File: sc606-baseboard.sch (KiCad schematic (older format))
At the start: 0 parts

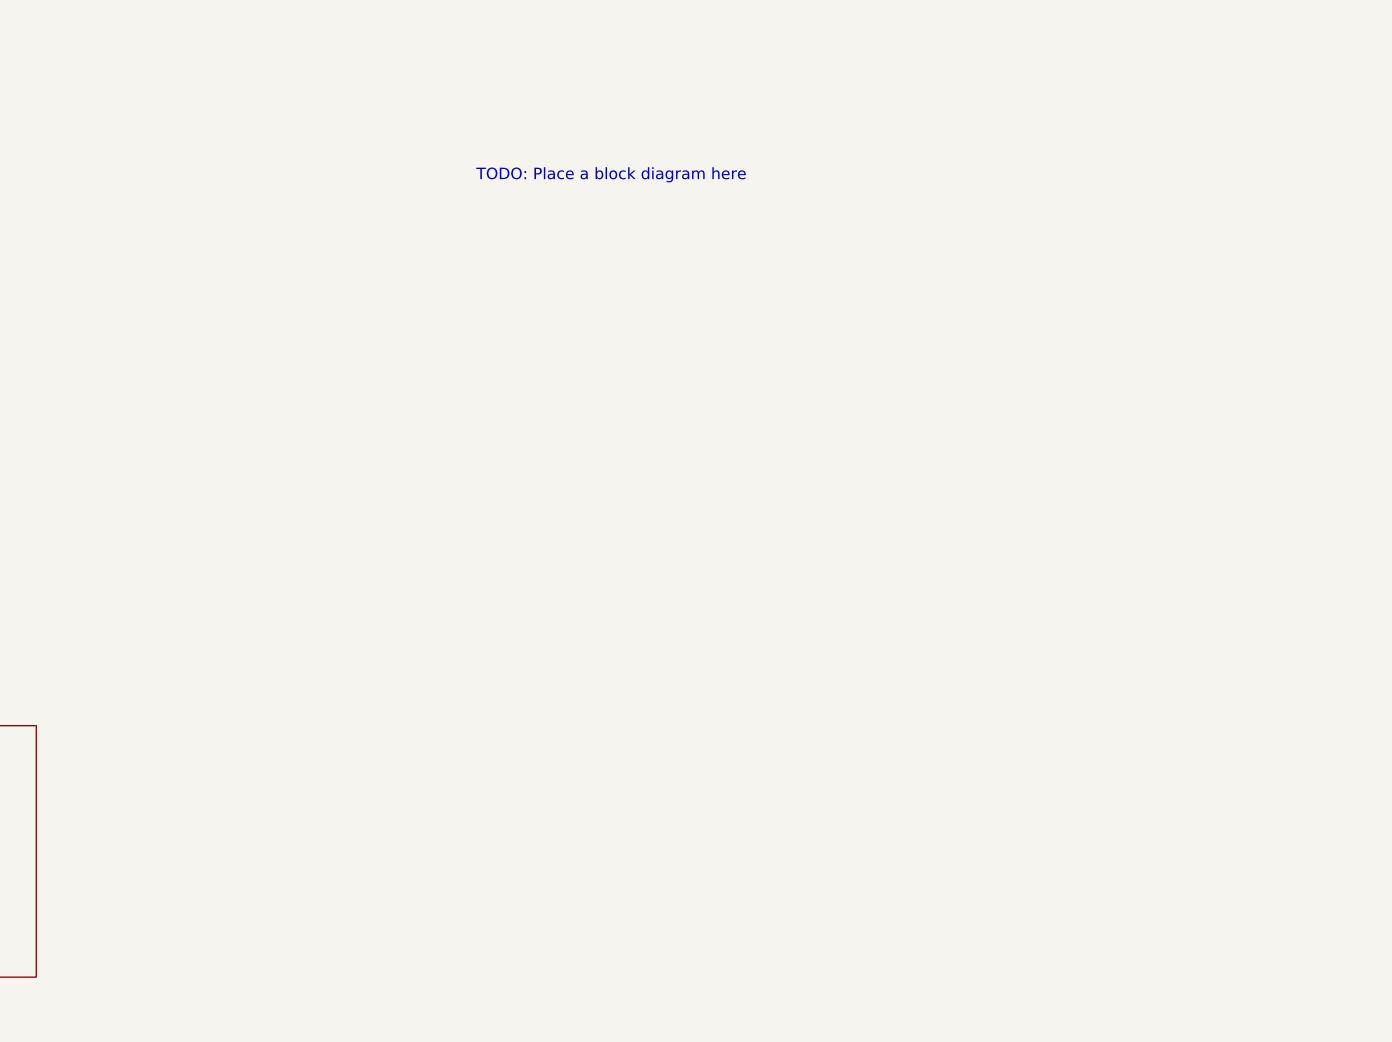
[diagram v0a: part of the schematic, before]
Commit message: update of block diagram, creation of sub-sheets
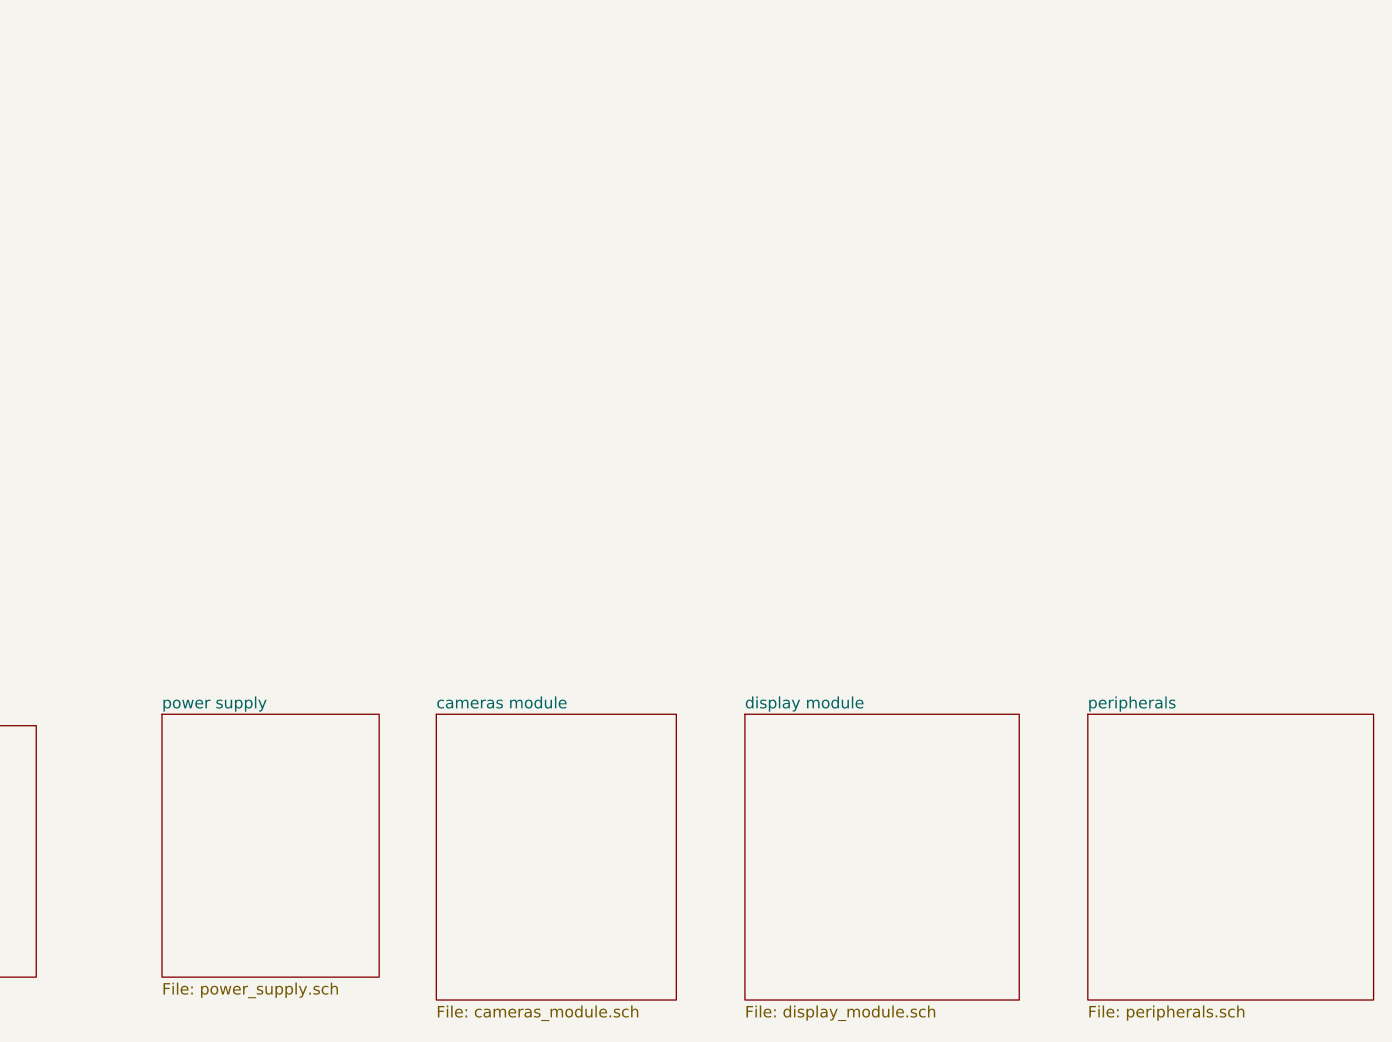
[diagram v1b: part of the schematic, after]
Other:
- note removed: "TODO: Place a block diagram here"

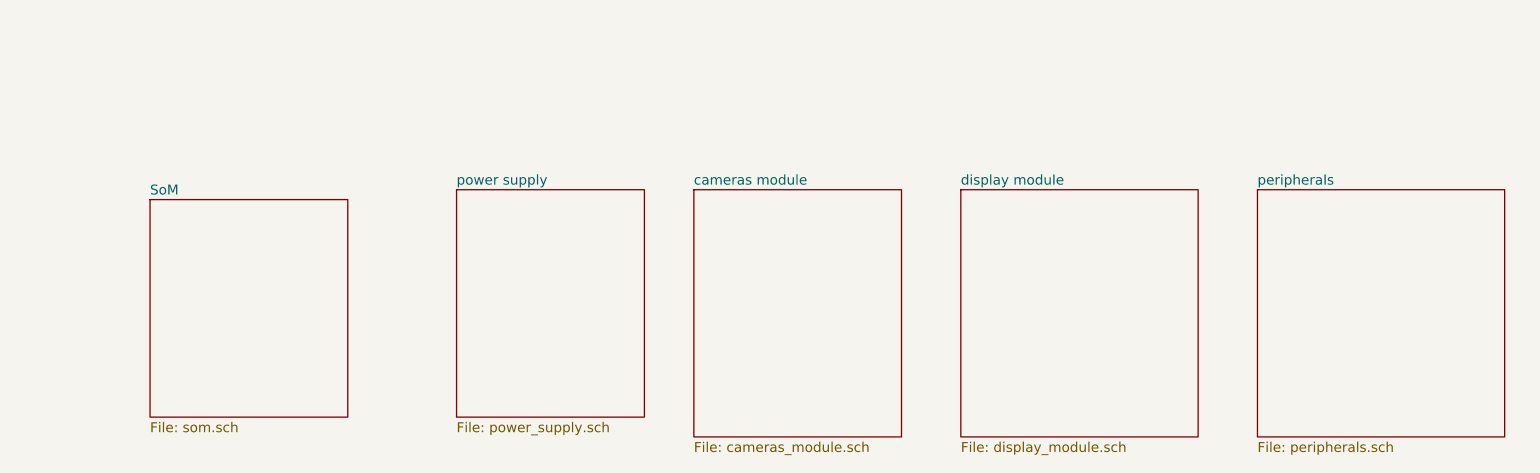
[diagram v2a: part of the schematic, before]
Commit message: Modifications after P. Szczygiel review
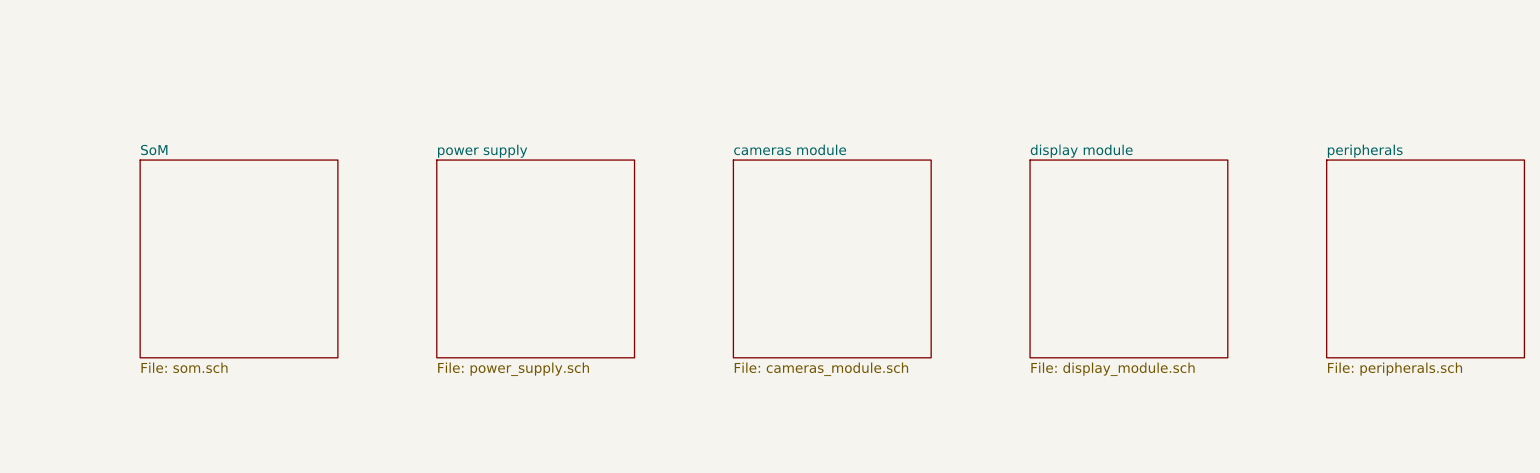
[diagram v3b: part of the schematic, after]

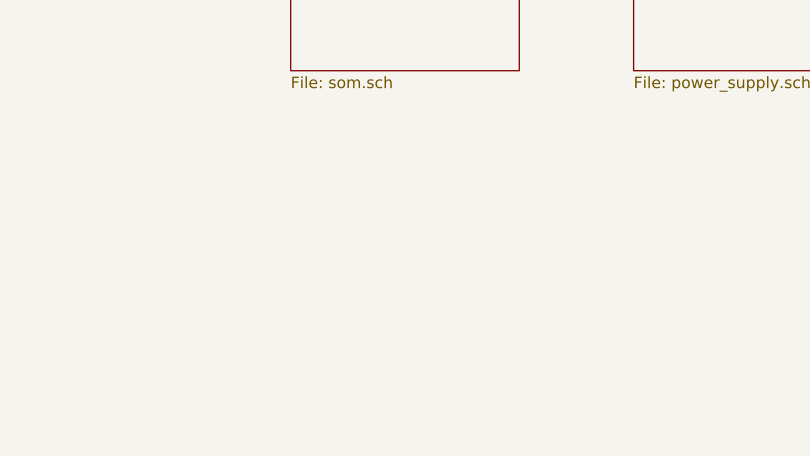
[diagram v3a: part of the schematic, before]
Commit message: Added ESD protection to HDMI
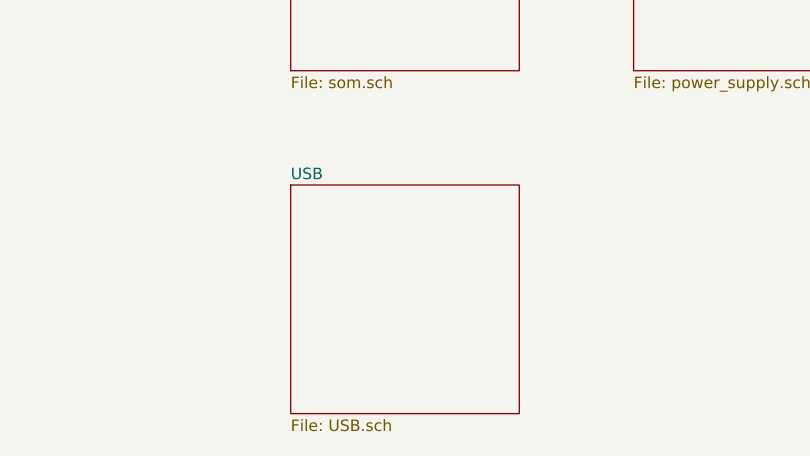
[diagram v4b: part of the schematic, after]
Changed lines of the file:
@@
 $Descr A3 16535 11693
 encoding utf-8
-Sheet 1 6
+Sheet 1 7
 Title ""
 Date "2022-01-04"
@@
 EndData
 $EndBitmap
+$Sheet
+S 5000 7500 1000 1000
+U 61F60810
+F0 "USB" 50
+F1 "USB.sch" 50
+$EndSheet
 $EndSCHEMATC

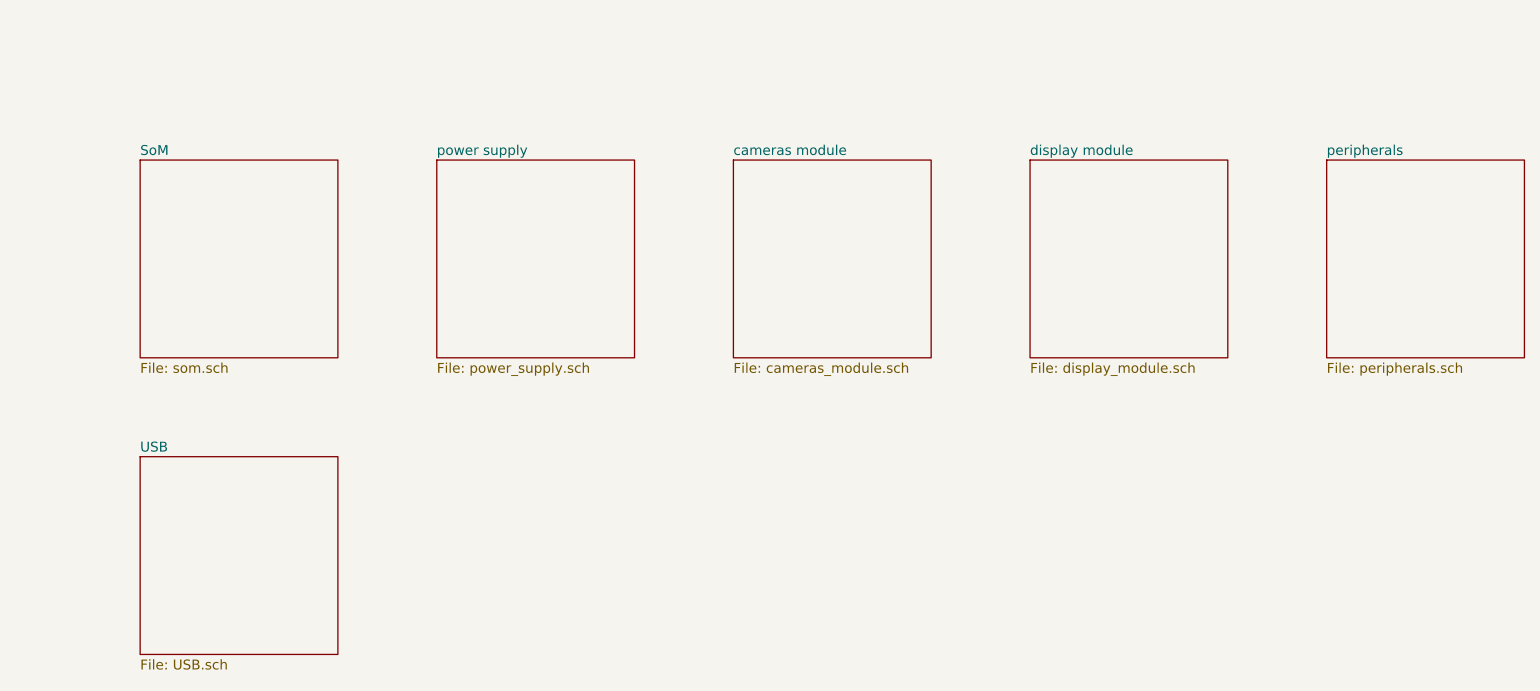
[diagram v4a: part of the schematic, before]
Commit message: Added USC-C connector and first option of debug UART
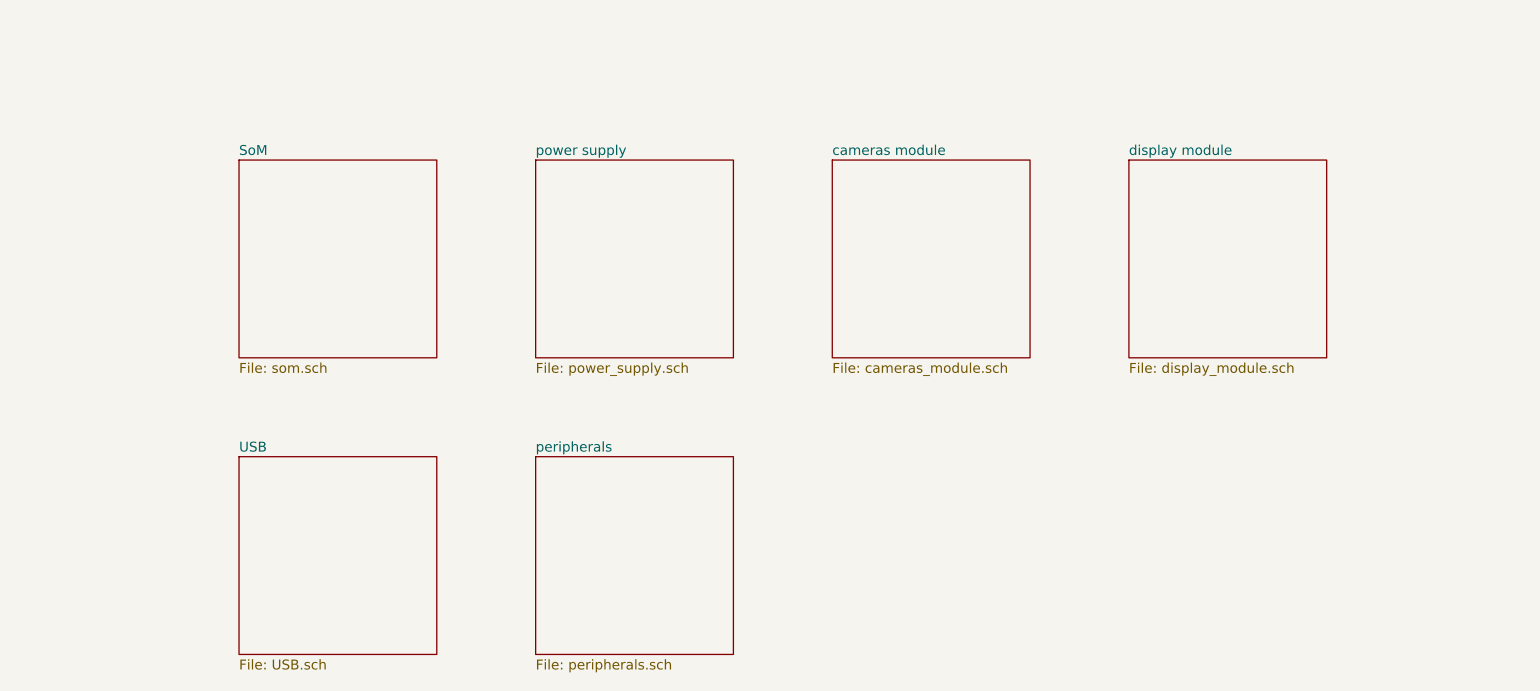
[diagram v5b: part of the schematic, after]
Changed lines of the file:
@@
 SC606T Baseboard
 $Sheet
-S 5000 6000 1000 1000
+S 5500 6000 1000 1000
 U 61D43102
 F0 "SoM" 50
@@
 $EndSheet
 $Sheet
-S 6500 6000 1000 1000
+S 7000 6000 1000 1000
 U 61D49F54
 F0 "power supply" 50
@@
 $EndSheet
 $Sheet
-S 8000 6000 1000 1000
+S 8500 6000 1000 1000
 U 61D49F95
 F0 "cameras module" 50
@@
 $EndSheet
 $Sheet
-S 9500 6000 1000 1000
+S 10000 6000 1000 1000
 U 61D49FBF
 F0 "display module" 50
@@
 $EndSheet
 $Sheet
-S 11000 6000 1000 1000
+S 7000 7500 1000 1000
 U 61D49FDE
 F0 "peripherals" 50
@@
 $EndBitmap
 $Sheet
-S 5000 7500 1000 1000
+S 5500 7500 1000 1000
 U 61F60810
 F0 "USB" 50
